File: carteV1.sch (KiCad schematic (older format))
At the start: 68 parts, among them J12 FILTER_IOUT_DUT2, J7 CRYSTAL OUTDUT2, P1 CONN_10, P3 CONN_2, T8 T1-1T, U1 AD9954, X1 25mhz

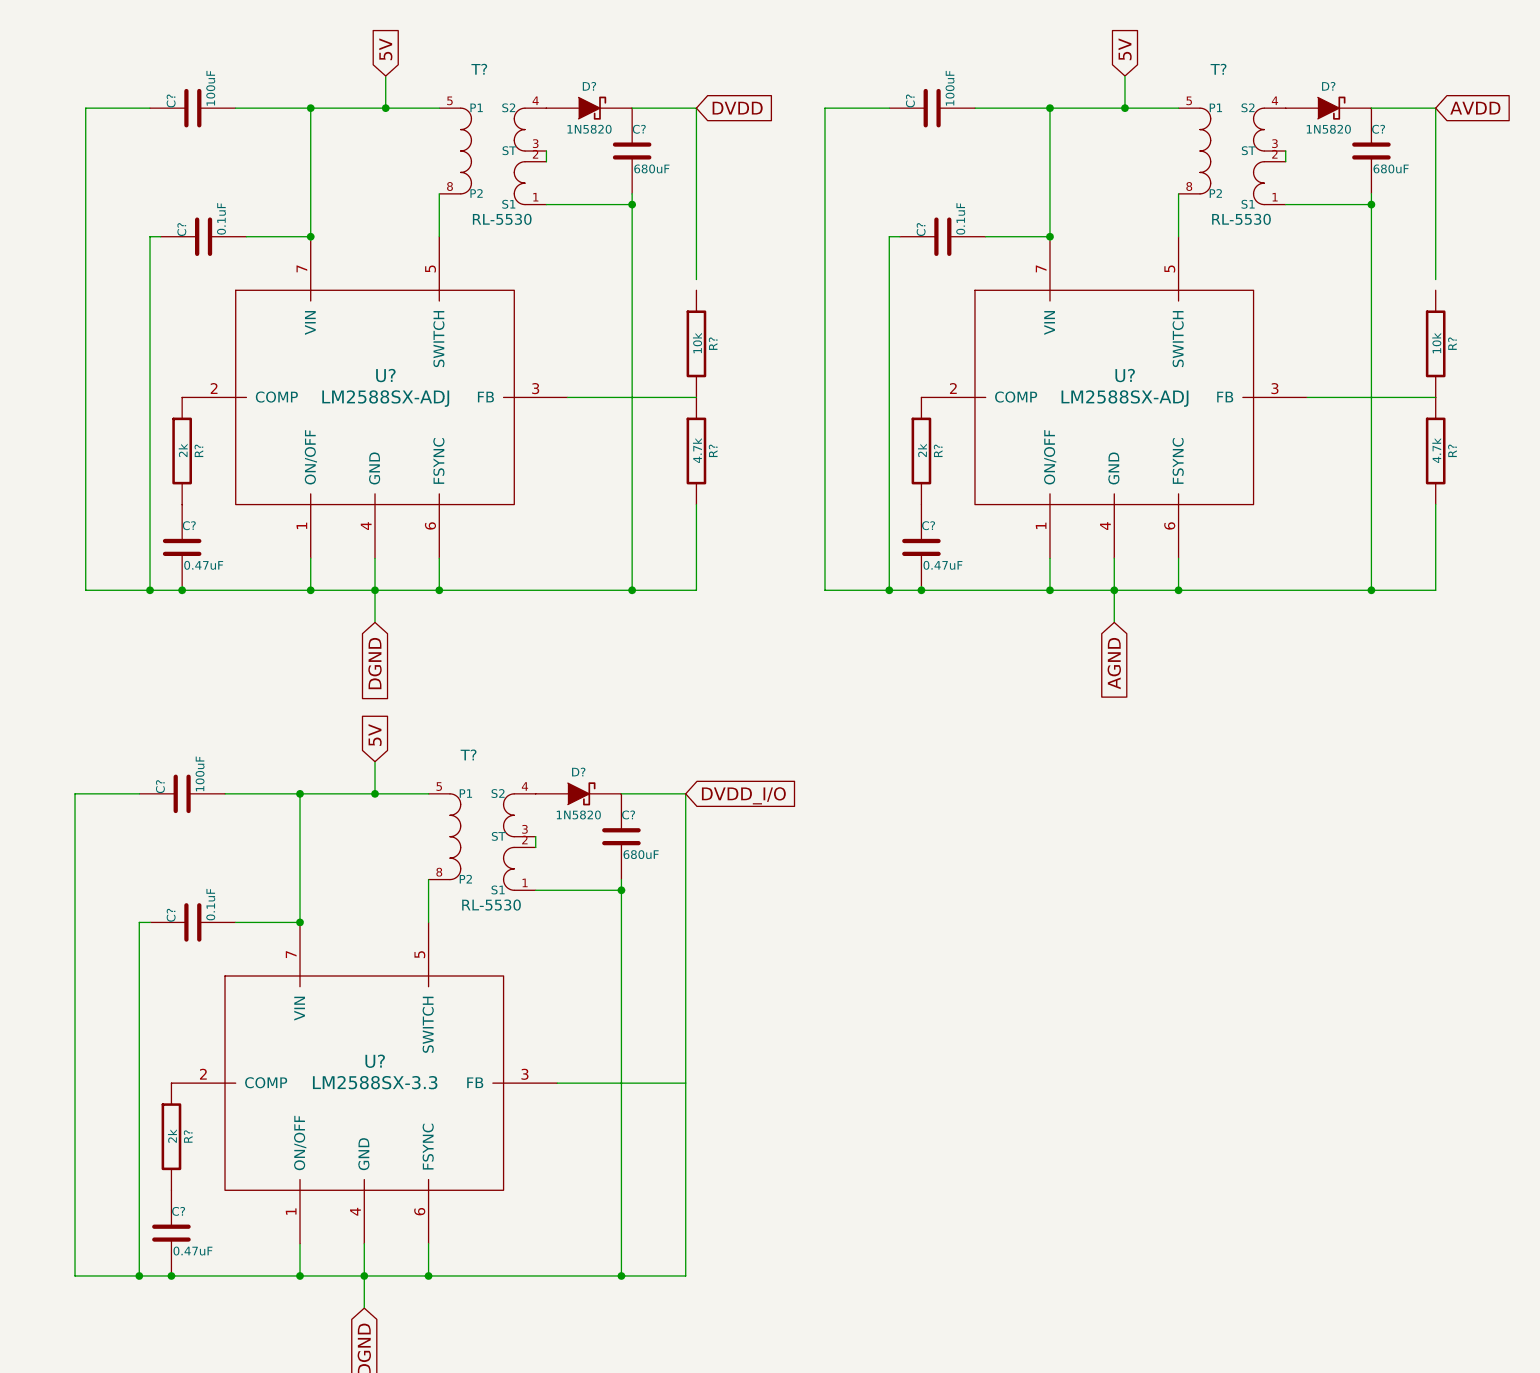
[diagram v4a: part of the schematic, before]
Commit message: Maj schéma structurel Kicad
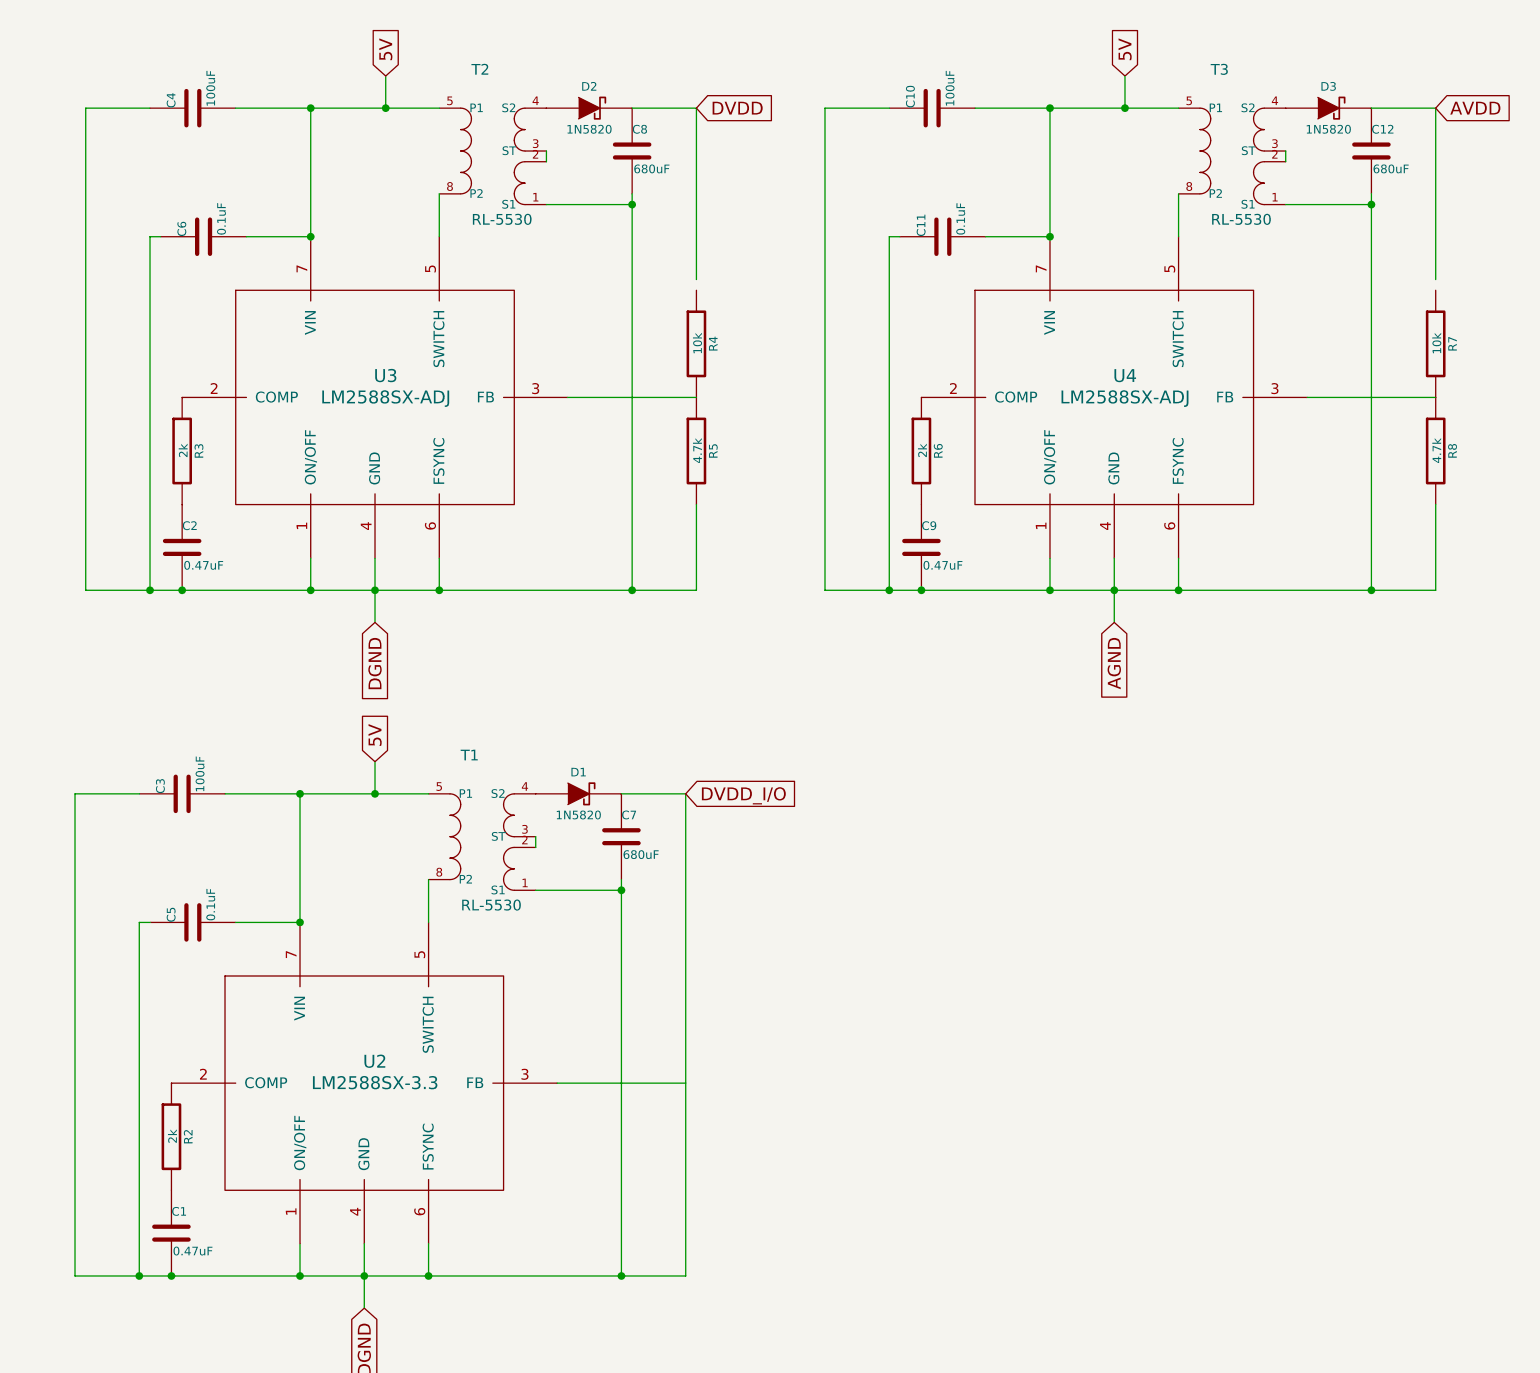
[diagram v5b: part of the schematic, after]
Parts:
- gave numbers to parts that had none: 28
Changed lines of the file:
@@
 LIBS:mcp2210
 LIBS:minicir
-LIBS:lm2588sx-adj
-LIBS:rl-5530
 LIBS:carteV1-cache
 EELAYER 27 0
@@
 $EndComp
 $Comp
-L R R?
+L R R5
 U 1 1 546C80BB
 P 11750 2400
-F 0 "R?" V 11830 2400 40  0000 C CNN
+F 0 "R5" V 11830 2400 40  0000 C CNN
 F 1 "4.7k" V 11757 2401 40  0000 C CNN
 F 2 "~" V 11680 2400 30  0000 C CNN
@@
 $EndComp
 $Comp
-L R R?
+L R R4
 U 1 1 546C80C1
 P 11750 1900
-F 0 "R?" V 11830 1900 40  0000 C CNN
+F 0 "R4" V 11830 1900 40  0000 C CNN
 F 1 "10k" V 11757 1901 40  0000 C CNN
 F 2 "~" V 11680 1900 30  0000 C CNN
@@
 $EndComp
 $Comp
-L R R?
+L R R3
 U 1 1 546C80D0
 P 9350 2400
-F 0 "R?" V 9430 2400 40  0000 C CNN
+F 0 "R3" V 9430 2400 40  0000 C CNN
 F 1 "2k" V 9357 2401 40  0000 C CNN
 F 2 "~" V 9280 2400 30  0000 C CNN
@@
 $EndComp
 $Comp
-L C C?
+L C C2
 U 1 1 546C80D6
 P 9350 2850
-F 0 "C?" H 9350 2950 40  0000 L CNN
+F 0 "C2" H 9350 2950 40  0000 L CNN
 F 1 "0.47uF" H 9356 2765 40  0000 L CNN
 F 2 "~" H 9388 2700 30  0000 C CNN
@@
 $EndComp
 $Comp
-L C C?
+L C C6
 U 1 1 546C80DC
 P 9450 1400
-F 0 "C?" H 9450 1500 40  0000 L CNN
+F 0 "C6" H 9450 1500 40  0000 L CNN
 F 1 "0.1uF" H 9456 1315 40  0000 L CNN
 F 2 "~" H 9488 1250 30  0000 C CNN
@@
 $EndComp
 $Comp
-L SS3P4 D?
+L SS3P4 D2
 U 1 1 546C80EA
 P 11250 800
-F 0 "D?" H 11250 900 40  0000 C CNN
+F 0 "D2" H 11250 900 40  0000 C CNN
 F 1 "1N5820" H 11250 700 40  0000 C CNN
 F 2 "" H 11250 800 60  0000 C CNN
@@
 $EndComp
 $Comp
-L C C?
+L C C8
 U 1 1 546C80F3
 P 11450 1000
-F 0 "C?" H 11450 1100 40  0000 L CNN
+F 0 "C8" H 11450 1100 40  0000 L CNN
 F 1 "680uF" H 11456 915 40  0000 L CNN
 F 2 "~" H 11488 850 30  0000 C CNN
@@
 $EndComp
 $Comp
-L C C?
+L C C4
 U 1 1 546C80FC
 P 9400 800
-F 0 "C?" H 9400 900 40  0000 L CNN
+F 0 "C4" H 9400 900 40  0000 L CNN
 F 1 "100uF" H 9406 715 40  0000 L CNN
 F 2 "~" H 9438 650 30  0000 C CNN
@@
 	9200 1400 9200 3050
 $Comp
-L RL-5530 T?
+L RL-5530 T2
 U 1 1 546CAECA
 P 10800 1000
-F 0 "T?" H 10700 1350 50  0000 L BNN
+F 0 "T2" H 10700 1350 50  0000 L BNN
 F 1 "RL-5530" H 10700 650 50  0000 L BNN
 F 2 "minicir-KK81" H 10800 1300 50  0001 C CNN
@@
 Connection ~ 11450 1250
 $Comp
-L LM2588SX-ADJ U?
+L LM2588SX-ADJ U3
 U 1 1 546C80B5
 P 10250 2000
-F 0 "U?" H 10300 1950 60  0000 C CNN
+F 0 "U3" H 10300 1950 60  0000 C CNN
 F 1 "LM2588SX-ADJ" H 10300 1850 60  0000 C CNN
 F 2 "~" H 10300 1950 60  0000 C CNN
@@
 Connection ~ 10300 800
 $Comp
-L R R?
+L R R8
 U 1 1 546CBE9B
 P 15200 2400
-F 0 "R?" V 15280 2400 40  0000 C CNN
+F 0 "R8" V 15280 2400 40  0000 C CNN
 F 1 "4.7k" V 15207 2401 40  0000 C CNN
 F 2 "~" V 15130 2400 30  0000 C CNN
@@
 $EndComp
 $Comp
-L R R?
+L R R7
 U 1 1 546CBEA1
 P 15200 1900
-F 0 "R?" V 15280 1900 40  0000 C CNN
+F 0 "R7" V 15280 1900 40  0000 C CNN
 F 1 "10k" V 15207 1901 40  0000 C CNN
 F 2 "~" V 15130 1900 30  0000 C CNN
@@
 $EndComp
 $Comp
-L R R?
+L R R6
 U 1 1 546CBEA7
 P 12800 2400
-F 0 "R?" V 12880 2400 40  0000 C CNN
+F 0 "R6" V 12880 2400 40  0000 C CNN
 F 1 "2k" V 12807 2401 40  0000 C CNN
 F 2 "~" V 12730 2400 30  0000 C CNN
@@
 $EndComp
 $Comp
-L C C?
+L C C9
 U 1 1 546CBEAD
 P 12800 2850
-F 0 "C?" H 12800 2950 40  0000 L CNN
+F 0 "C9" H 12800 2950 40  0000 L CNN
 F 1 "0.47uF" H 12806 2765 40  0000 L CNN
 F 2 "~" H 12838 2700 30  0000 C CNN
@@
 $EndComp
 $Comp
-L C C?
+L C C11
 U 1 1 546CBEB3
 P 12900 1400
-F 0 "C?" H 12900 1500 40  0000 L CNN
+F 0 "C11" H 12900 1500 40  0000 L CNN
 F 1 "0.1uF" H 12906 1315 40  0000 L CNN
 F 2 "~" H 12938 1250 30  0000 C CNN
@@
 $EndComp
 $Comp
-L SS3P4 D?
+L SS3P4 D3
 U 1 1 546CBEB9
 P 14700 800
-F 0 "D?" H 14700 900 40  0000 C CNN
+F 0 "D3" H 14700 900 40  0000 C CNN
 F 1 "1N5820" H 14700 700 40  0000 C CNN
 F 2 "" H 14700 800 60  0000 C CNN
@@
 $EndComp
 $Comp
-L C C?
+L C C12
 U 1 1 546CBEBF
 P 14900 1000
-F 0 "C?" H 14900 1100 40  0000 L CNN
+F 0 "C12" H 14900 1100 40  0000 L CNN
 F 1 "680uF" H 14906 915 40  0000 L CNN
 F 2 "~" H 14938 850 30  0000 C CNN
@@
 $EndComp
 $Comp
-L C C?
+L C C10
 U 1 1 546CBEC5
 P 12850 800
-F 0 "C?" H 12850 900 40  0000 L CNN
+F 0 "C10" H 12850 900 40  0000 L CNN
 F 1 "100uF" H 12856 715 40  0000 L CNN
 F 2 "~" H 12888 650 30  0000 C CNN
@@
 	12650 1400 12650 3050
 $Comp
-L RL-5530 T?
+L RL-5530 T3
 U 1 1 546CBED7
 P 14250 1000
-F 0 "T?" H 14150 1350 50  0000 L BNN
+F 0 "T3" H 14150 1350 50  0000 L BNN
 F 1 "RL-5530" H 14150 650 50  0000 L BNN
 F 2 "minicir-KK81" H 14250 1300 50  0001 C CNN
@@
 Connection ~ 14900 1250
 $Comp
-L LM2588SX-ADJ U?
+L LM2588SX-ADJ U4
 U 1 1 546CBEE7
 P 13700 2000
-F 0 "U?" H 13750 1950 60  0000 C CNN
+F 0 "U4" H 13750 1950 60  0000 C CNN
 F 1 "LM2588SX-ADJ" H 13750 1850 60  0000 C CNN
 F 2 "~" H 13750 1950 60  0000 C CNN
@@
 Connection ~ 13750 800
 $Comp
-L R R?
+L R R2
 U 1 1 546CBF06
 P 9300 5600
-F 0 "R?" V 9380 5600 40  0000 C CNN
+F 0 "R2" V 9380 5600 40  0000 C CNN
 F 1 "2k" V 9307 5601 40  0000 C CNN
 F 2 "~" V 9230 5600 30  0000 C CNN
@@
 $EndComp
 $Comp
-L C C?
+L C C1
 U 1 1 546CBF0C
 P 9300 6050
-F 0 "C?" H 9300 6150 40  0000 L CNN
+F 0 "C1" H 9300 6150 40  0000 L CNN
 F 1 "0.47uF" H 9306 5965 40  0000 L CNN
 F 2 "~" H 9338 5900 30  0000 C CNN
@@
 $EndComp
 $Comp
-L C C?
+L C C5
 U 1 1 546CBF12
 P 9400 4600
-F 0 "C?" H 9400 4700 40  0000 L CNN
+F 0 "C5" H 9400 4700 40  0000 L CNN
 F 1 "0.1uF" H 9406 4515 40  0000 L CNN
 F 2 "~" H 9438 4450 30  0000 C CNN
@@
 $EndComp
 $Comp
-L SS3P4 D?
+L SS3P4 D1
 U 1 1 546CBF18
 P 11200 4000
-F 0 "D?" H 11200 4100 40  0000 C CNN
+F 0 "D1" H 11200 4100 40  0000 C CNN
 F 1 "1N5820" H 11200 3900 40  0000 C CNN
 F 2 "" H 11200 4000 60  0000 C CNN
@@
 $EndComp
 $Comp
-L C C?
+L C C7
 U 1 1 546CBF1E
 P 11400 4200
-F 0 "C?" H 11400 4300 40  0000 L CNN
+F 0 "C7" H 11400 4300 40  0000 L CNN
 F 1 "680uF" H 11406 4115 40  0000 L CNN
 F 2 "~" H 11438 4050 30  0000 C CNN
@@
 $EndComp
 $Comp
-L C C?
+L C C3
 U 1 1 546CBF24
 P 9350 4000
-F 0 "C?" H 9350 4100 40  0000 L CNN
+F 0 "C3" H 9350 4100 40  0000 L CNN
 F 1 "100uF" H 9356 3915 40  0000 L CNN
 F 2 "~" H 9388 3850 30  0000 C CNN
@@
 	9150 4600 9150 6250
 $Comp
-L RL-5530 T?
+L RL-5530 T1
 U 1 1 546CBF36
 P 10750 4200
-F 0 "T?" H 10650 4550 50  0000 L BNN
+F 0 "T1" H 10650 4550 50  0000 L BNN
 F 1 "RL-5530" H 10650 3850 50  0000 L BNN
 F 2 "minicir-KK81" H 10750 4500 50  0001 C CNN
@@
 Connection ~ 10250 4000
 $Comp
-L LM2588SX-ADJ U?
+L LM2588SX-ADJ U2
 U 1 1 546CBF46
 P 10200 5200
-F 0 "U?" H 10250 5150 60  0000 C CNN
+F 0 "U2" H 10250 5150 60  0000 C CNN
 F 1 "LM2588SX-3.3" H 10250 5050 60  0000 C CNN
 F 2 "~" H 10250 5150 60  0000 C CNN
